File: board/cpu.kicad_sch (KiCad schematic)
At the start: 6 parts, among them U1 MC68000P

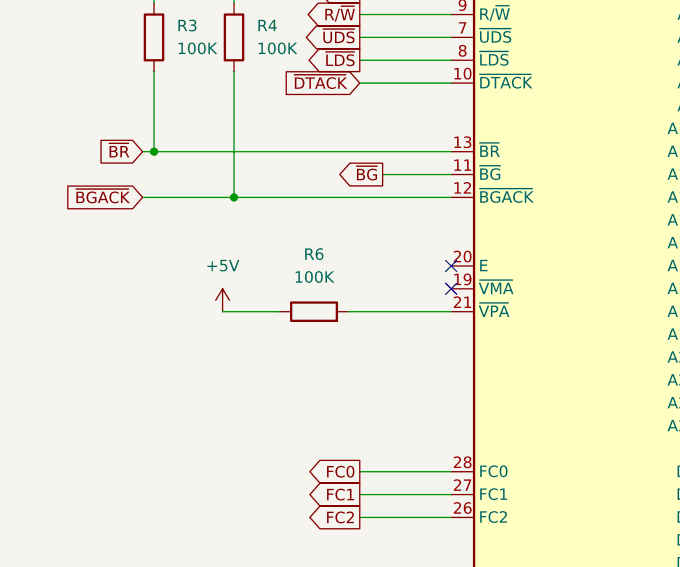
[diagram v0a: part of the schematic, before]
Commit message: Run VPA from GLUE to CPU
* delete old ENGINE_IACK line and pullup - interrupts will be autovectored
* run VPA between GLUE and CPU
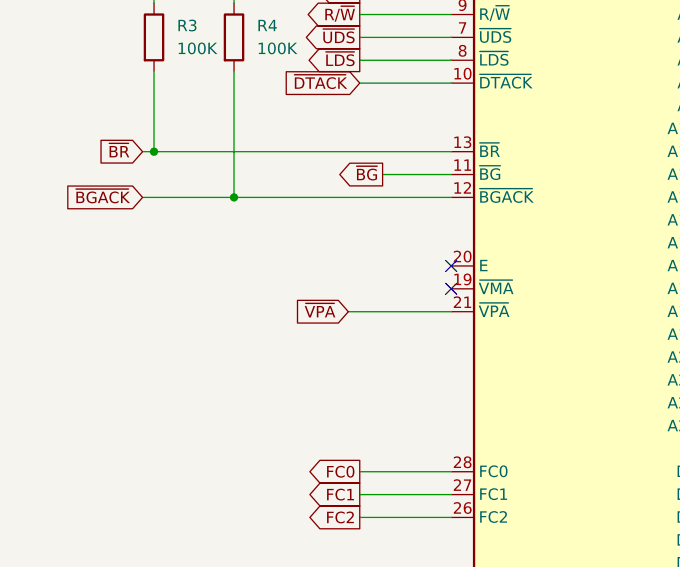
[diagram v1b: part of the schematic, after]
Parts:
- removed R6: 100K, Resistor_THT:R_Axial_DIN0207_L6.3mm_D2.5mm_P10.16mm_Horizontal, symbol Device:R
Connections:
- net ~{VPA}: now reaches U1.21 (~{VPA})
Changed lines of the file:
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@@
 	(wire
 		(pts
-			(xy 124.46 80.01) (xy 118.11 80.01)
+			(xy 158.75 26.67) (xy 158.75 31.75)
 		)
 		(stroke
@@
 	(wire
 		(pts
-			(xy 158.75 26.67) (xy 158.75 31.75)
+			(xy 133.35 54.61) (xy 143.51 54.61)
 		)
 		(stroke
@@
 	(wire
 		(pts
-			(xy 133.35 54.61) (xy 143.51 54.61)
+			(xy 137.16 152.4) (xy 152.4 152.4)
 		)
 		(stroke
@@
 	(wire
 		(pts
-			(xy 137.16 152.4) (xy 152.4 152.4)
+			(xy 173.99 92.71) (xy 184.15 92.71)
 		)
 		(stroke
@@
 	(wire
 		(pts
-			(xy 173.99 92.71) (xy 184.15 92.71)
+			(xy 133.35 44.45) (xy 143.51 44.45)
 		)
 		(stroke
@@
 	(wire
 		(pts
-			(xy 133.35 44.45) (xy 143.51 44.45)
+			(xy 133.35 52.07) (xy 143.51 52.07)
 		)
 		(stroke
@@
 	(wire
 		(pts
-			(xy 133.35 52.07) (xy 143.51 52.07)
+			(xy 173.99 44.45) (xy 184.15 44.45)
 		)
 		(stroke
@@
 	(wire
 		(pts
-			(xy 173.99 44.45) (xy 184.15 44.45)
+			(xy 173.99 80.01) (xy 184.15 80.01)
 		)
 		(stroke
@@
 	(wire
 		(pts
-			(xy 173.99 80.01) (xy 184.15 80.01)
+			(xy 133.35 128.27) (xy 143.51 128.27)
 		)
 		(stroke
@@
 	(wire
 		(pts
-			(xy 133.35 128.27) (xy 143.51 128.27)
+			(xy 119.38 43.18) (xy 119.38 45.72)
 		)
 		(stroke
@@
 	(wire
 		(pts
-			(xy 119.38 43.18) (xy 119.38 45.72)
+			(xy 137.16 160.02) (xy 152.4 160.02)
 		)
 		(stroke
@@
 	(wire
 		(pts
-			(xy 137.16 160.02) (xy 152.4 160.02)
+			(xy 173.99 100.33) (xy 184.15 100.33)
 		)
 		(stroke
@@
 	(wire
 		(pts
-			(xy 173.99 100.33) (xy 184.15 100.33)
+			(xy 133.35 49.53) (xy 143.51 49.53)
 		)
 		(stroke
@@
 	(wire
 		(pts
-			(xy 133.35 49.53) (xy 143.51 49.53)
+			(xy 173.99 39.37) (xy 184.15 39.37)
 		)
 		(stroke
@@
 	(wire
 		(pts
-			(xy 173.99 39.37) (xy 184.15 39.37)
+			(xy 173.99 135.89) (xy 184.15 135.89)
 		)
 		(stroke
@@
 		)
 	)
-	(wire
-		(pts
-			(xy 173.99 135.89) (xy 184.15 135.89)
-		)
-		(stroke
-			(width 0)
-			(type default)
-		)
-	)
 	(global_label "A12"
 		(shape output)
@@
 				)
 				(justify left)
+				(hide yes)
+			)
+		)
+	)
+	(global_label "~{VPA}"
+		(shape input)
+		(at 132.08 80.01 180)
+		(fields_autoplaced yes)
+		(effects
+			(font
+				(size 1.27 1.27)
+			)
+			(justify right)
+		)
+		(property "Intersheetrefs" "${INTERSHEET_REFS}"
+			(at 125.6476 80.01 0)
+			(effects
+				(font
+					(size 1.27 1.27)
+				)
+				(justify right)
 				(hide yes)
 			)
@@
 				(path "/afefa398-9f39-4b22-97f8-dae9b102df0d/e2759770-a9ef-4fa2-921d-b35f031ff7ee"
 					(reference "#PWR016")
-					(unit 1)
-				)
-			)
-		)
-	)
-	(symbol
-		(lib_id "power:+5V")
-		(at 118.11 80.01 0)
-		(unit 1)
-		(exclude_from_sim no)
-		(in_bom yes)
-		(on_board yes)
-		(dnp no)
-		(fields_autoplaced yes)
-		(property "Reference" "#PWR015"
-			(at 118.11 83.82 0)
-			(effects
-				(font
-					(size 1.27 1.27)
-				)
-				(hide yes)
-			)
-		)
-		(property "Value" "+5V"
-			(at 118.11 74.93 0)
-			(effects
-				(font
-					(size 1.27 1.27)
-				)
-			)
-		)
-		(property "Footprint" ""
-			(at 118.11 80.01 0)
-			(effects
-				(font
-					(size 1.27 1.27)
-				)
-				(hide yes)
-			)
-		)
-		(property "Datasheet" ""
-			(at 118.11 80.01 0)
-			(effects
-				(font
-					(size 1.27 1.27)
-				)
-				(hide yes)
-			)
-		)
-		(property "Description" "Power symbol creates a global label with name \"+5V\""
-			(at 118.11 80.01 0)
-			(effects
-				(font
-					(size 1.27 1.27)
-				)
-				(hide yes)
-			)
-		)
-		(pin "1"
-		)
-		(instances
-			(project "board"
-				(path "/afefa398-9f39-4b22-97f8-dae9b102df0d/e2759770-a9ef-4fa2-921d-b35f031ff7ee"
-					(reference "#PWR015")
 					(unit 1)
 				)
@@
 					(unit 1)
 				)
-			)
-		)
-	)
-	(symbol
-		(lib_id "Device:R")
-		(at 128.27 80.01 90)
-		(unit 1)
-		(exclude_from_sim no)
-		(in_bom yes)
-		(on_board yes)
-		(dnp no)
-		(fields_autoplaced yes)
-		(property "Reference" "R6"
-			(at 128.27 73.66 90)
-			(effects
-				(font
-					(size 1.27 1.27)
-				)
-			)
-		)
-		(property "Value" "100K"
-			(at 128.27 76.2 90)
-			(effects
-				(font
-					(size 1.27 1.27)
-				)
-			)
-		)
-		(property "Footprint" "Resistor_THT:R_Axial_DIN0207_L6.3mm_D2.5mm_P10.16mm_Horizontal"
-			(at 128.27 81.788 90)
-			(effects
-				(font
-					(size 1.27 1.27)
-				)
-				(hide yes)
-			)
-		)
-		(property "Datasheet" "~"
-			(at 128.27 80.01 0)
-			(effects
-				(font
-					(size 1.27 1.27)
-				)
-				(hide yes)
-			)
-		)
-		(property "Description" "Resistor"
-			(at 128.27 80.01 0)
-			(effects
-				(font
-					(size 1.27 1.27)
-				)
-				(hide yes)
-			)
-		)
-		(pin "1"
-		)
-		(pin "2"
-		)
-		(instances
-			(project ""
-				(path "/afefa398-9f39-4b22-97f8-dae9b102df0d/e2759770-a9ef-4fa2-921d-b35f031ff7ee"
-					(reference "R6")
-					(unit 1)
-				)

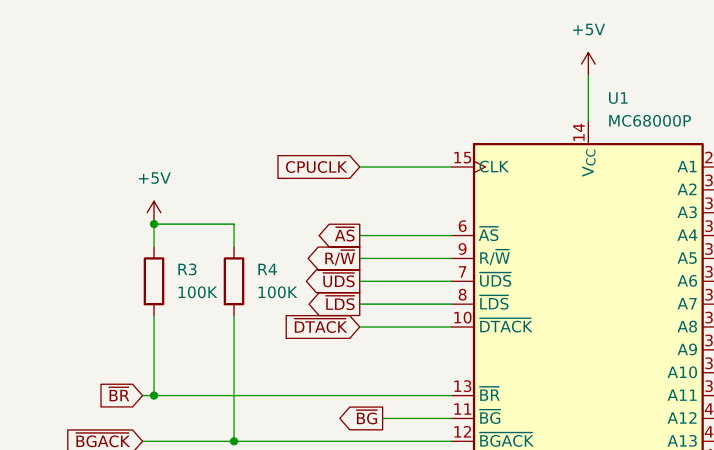
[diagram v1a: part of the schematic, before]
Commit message: CPUCLK -> SYSCLK
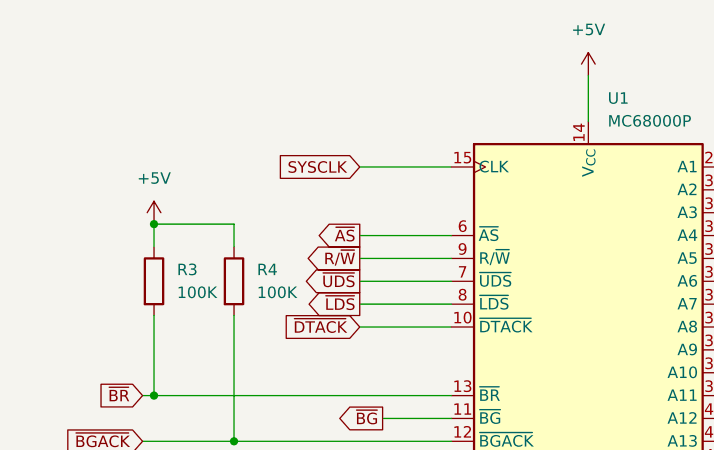
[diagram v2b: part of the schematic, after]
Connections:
- net CPUCLK renamed SYSCLK
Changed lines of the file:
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@@
 		)
 	)
-	(global_label "CPUCLK"
+	(global_label "SYSCLK"
 		(shape input)
 		(at 133.35 36.83 180)
